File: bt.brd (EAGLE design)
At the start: 100 x 80 mm, 19 parts, among them IC1 BLUETOOTH-RN42 HID, Q1 MOSFET-NCHANNELSMD, Q2 MOSFET-NCHANNELSMD, U1 MCP73831, X1 Micro USB

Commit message: Starting to flesh this out
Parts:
- removed C3, C4: 4.7uF, SparkFun:0402-CAP
- removed D11: RED, SparkFun:LED-0603
- removed JP7: LiPo Battery, SparkFun:JST-2-SMD
- removed JP8: (no value), SparkFun:1X02
- removed U1: MCP73831, SparkFun:SOT23-5
- removed X1: Micro USB, SparkFun:USB-MICROB
- added D1, D2: (no value), SparkFun-LED:LED-1206
- added JP1: RA 6Pin SMD, SparkFun-Connectors:1X06-SMD
- added JP2: (no value), SparkFun-Connectors:1X06-SMD-FEMALE-V2
- R2, R3, R4, R5, R7: value 10K -> 10k; device SparkFun:0603-RES -> SparkFun-Resistors:0805
- R6: value 330 -> 10k; device SparkFun:0402-RES -> SparkFun-Resistors:0805
- R8: value 10K -> 330; device SparkFun:0603-RES -> SparkFun-Resistors:0805
- R9: value 2K -> 330; device SparkFun:0402-RES -> SparkFun-Resistors:0805
- moved R9 79.5 mm to (25.4, 17.8), flipped to the bottom, turned to 180 degrees
- moved R6 56.1 mm to (14.0, 5.08), flipped to the bottom, turned to 270 degrees
- moved R8 49.3 mm to (20.3, 17.8), flipped to the bottom
- moved R7 49.1 mm to (15.2, 17.8), flipped to the bottom
- moved R1 46.6 mm to (17.8, 12.7), flipped to the bottom, turned to 270 degrees
- moved R3 41.3 mm to (14.0, 14.0), flipped to the bottom, turned to 270 degrees
- moved R2 36.4 mm to (17.8, 6.35), flipped to the bottom, turned to 270 degrees
- moved R4 35.8 mm to (14.0, 8.89), flipped to the bottom, turned to 270 degrees
- moved R5 35.1 mm to (10.2, 3.81), flipped to the bottom, turned to 180 degrees
- moved Q1 31.4 mm to (10.2, 12.7), flipped to the bottom, turned to 180 degrees
- moved Q2 31.4 mm to (10.2, 7.62), flipped to the bottom
- moved IC1 16.6 mm to (17.8, 8.89)
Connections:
- removed net CTS: R2.1
- removed net CTS_5V: R2.2
- removed net N$11: IC1.11
- removed net N$12: D11.A, R6.1
- removed net N$4: IC1.16
- removed net N$5: IC1.18
- removed net N$6: IC1.17
- removed net PROG: R9.1, U1.5
- removed net RTS: Q2.2, R7.2
- removed net RTS_5V: Q2.3, R8.2
- removed net RX: R5.1
- removed net RX_5V: R5.2
- removed net STAT: D11.C, U1.1
- removed net TX: Q1.2, R3.2
- removed net TX_5V: Q1.3, R4.2
- removed net VIN: C3.1, R6.2, U1.4, X1.VBUS
- new net UART_CTS: IC1.16, R2.1
- new net UART_CTS_5V: JP1.5, R2.2
- new net UART_RTS: IC1.15, Q2.2, R5.1
- new net UART_RTS_5V: JP1.2, Q2.3, R6.1
- new net UART_RX: IC1.13, R1.1
- new net UART_RX_5V: JP1.3, R1.2
- new net UART_TX: IC1.14, Q1.2, R3.1
- new net UART_TX_5V: JP1.4, Q1.3, R4.1
- new net USB_D+: IC1.17, JP2.4
- new net USB_D-: IC1.18, JP2.3
- net 3.3V: now also JP2.6, R3.2, R5.2; no longer R3.1, R7.1
- net GND: now also JP1.1, JP2.1, R7.1, R8.1, R9.1; no longer C3.2, C4.2, JP7.1, JP8.1, R9.2, U1.2, X1.GND
- net N$1: now also D2.C, R8.2; no longer IC1.13
- net N$10: now also D2.A
- net N$2: now also JP2.2; no longer IC1.14
- net N$3: now also D1.C, R9.2; no longer IC1.15
- net N$8: now also D1.A
- net N$9: now also R7.2
- net VCC: now also IC1.11, JP1.6, JP2.5, R4.2, R6.2; no longer C4.1, JP7.2, JP8.2, R4.1, R8.1, U1.3
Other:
- board size 100 x 80 mm -> 28.9 x 20.3 mm

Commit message: More updates
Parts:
- JP1: value RA 6Pin SMD -> (none); device SparkFun-Connectors:1X06-SMD -> SparkFun-Connectors:1X06-SMD-FEMALE-V2
- JP2: value (none) -> RA 6Pin SMD; device SparkFun-Connectors:1X06-SMD-FEMALE-V2 -> SparkFun-Connectors:1X06-SMD
- moved R2 12.8 mm to (12.1, 17.8), turned to 0 degrees
- moved R3 11.9 mm to (17.1, 2.54)
- moved R5 11.7 mm to (14.6, 14.6), turned to 270 degrees
- moved R6 10.0 mm to (17.1, 14.6)
- moved Q1 8.08 mm to (15.9, 6.99)
- moved Q2 6.54 mm to (15.9, 10.8), turned to 180 degrees
- moved R4 6.38 mm to (14.6, 2.54)
- moved R1 5.43 mm to (15.9, 17.8), turned to 0 degrees
- moved R7 5.08 mm to (20.3, 17.8), turned to 180 degrees
- moved JP2 3.86 mm to (6.35, 9.53)
- moved R8 3.81 mm to (16.5, 17.8), flipped to the top, turned to 180 degrees
- moved D2 3.18 mm to (12.1, 17.8), turned to 0 degrees
- moved JP1 2.62 mm to (24.1, 9.53)
- moved R9 1.27 mm to (26.7, 17.8), flipped to the top
- moved D1 1.27 mm to (21.6, 17.8)
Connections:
- removed net N$2: JP2.2
- net 3.3V: now also JP1.6; no longer JP2.6
- net UART_CTS_5V: now also JP2.5; no longer JP1.5
- net UART_RTS_5V: now also JP2.2; no longer JP1.2
- net UART_RX_5V: now also JP2.3; no longer JP1.3
- net UART_TX_5V: now also JP2.4; no longer JP1.4
- net USB_D+: now also JP1.4; no longer JP2.4
- net USB_D-: now also JP1.3; no longer JP2.3
- net VCC: now also JP1.5, JP2.6; no longer JP1.6, JP2.5
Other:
- board size 28.9 x 20.3 mm -> 21.3 x 19.7 mm
- board text added: "3.3V"
- board text added: "CTS"
- board text added: "D+"
- board text added: "D-"
- board text added: "GND"
- board text added: "NC"
- board text added: "RTS"
- board text added: "RX"
- board text added: "TX"
- board text added: "VCC"

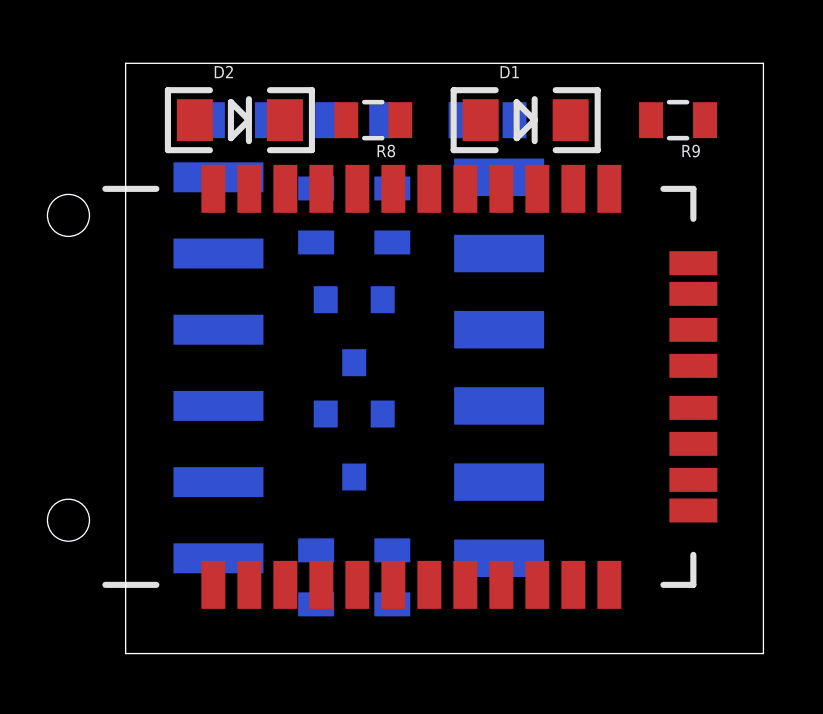
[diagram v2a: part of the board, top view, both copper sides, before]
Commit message: Tried to route the BT board.... Do I need 4 layers for this?
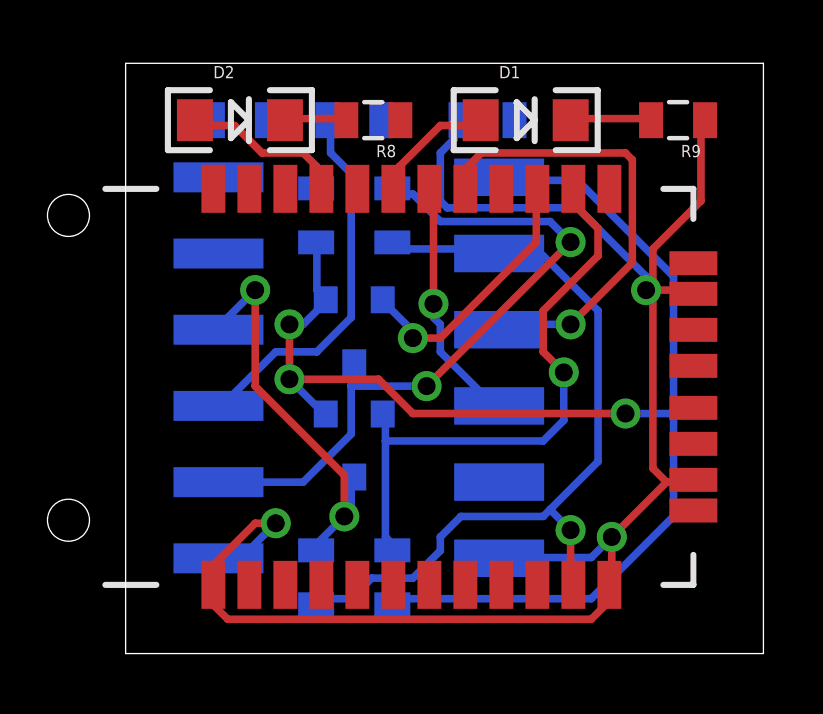
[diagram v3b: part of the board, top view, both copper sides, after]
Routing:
- net GND: track 0.00 -> 55.7 mm, vias 0 -> 3
- net 3.3V: track 0.00 -> 46.3 mm, vias 0 -> 3
- net VCC: track 0.00 -> 27.5 mm, vias 0 -> 1
- net UART_RTS_5V: track 0.00 -> 23.6 mm, vias 0 -> 2
- net UART_TX: track 0.00 -> 20.0 mm, vias 0 -> 1
- net USB_D+: track 0.00 -> 15.4 mm, vias 0 -> 1
- net UART_TX_5V: track 0.00 -> 13.5 mm, vias 0 -> 2
- net UART_RX_5V: track 0.00 -> 12.6 mm
- net UART_RTS: track 0.00 -> 8.90 mm, vias 0 -> 1
- net USB_D-: track 0.00 -> 8.29 mm, vias 0 -> 1
- net N$10: track 0.00 -> 5.55 mm
- net N$8: track 0.00 -> 4.24 mm
- net N$3: track 0.00 -> 2.69 mm
- net N$1: track 0.00 -> 2.07 mm
